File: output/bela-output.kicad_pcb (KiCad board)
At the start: 2 copper layers, 55 parts, among them P1 in_bela, P2 MTA-156-4, P3 out_mod, U1 TL074, U2 TL074, U3 TL072

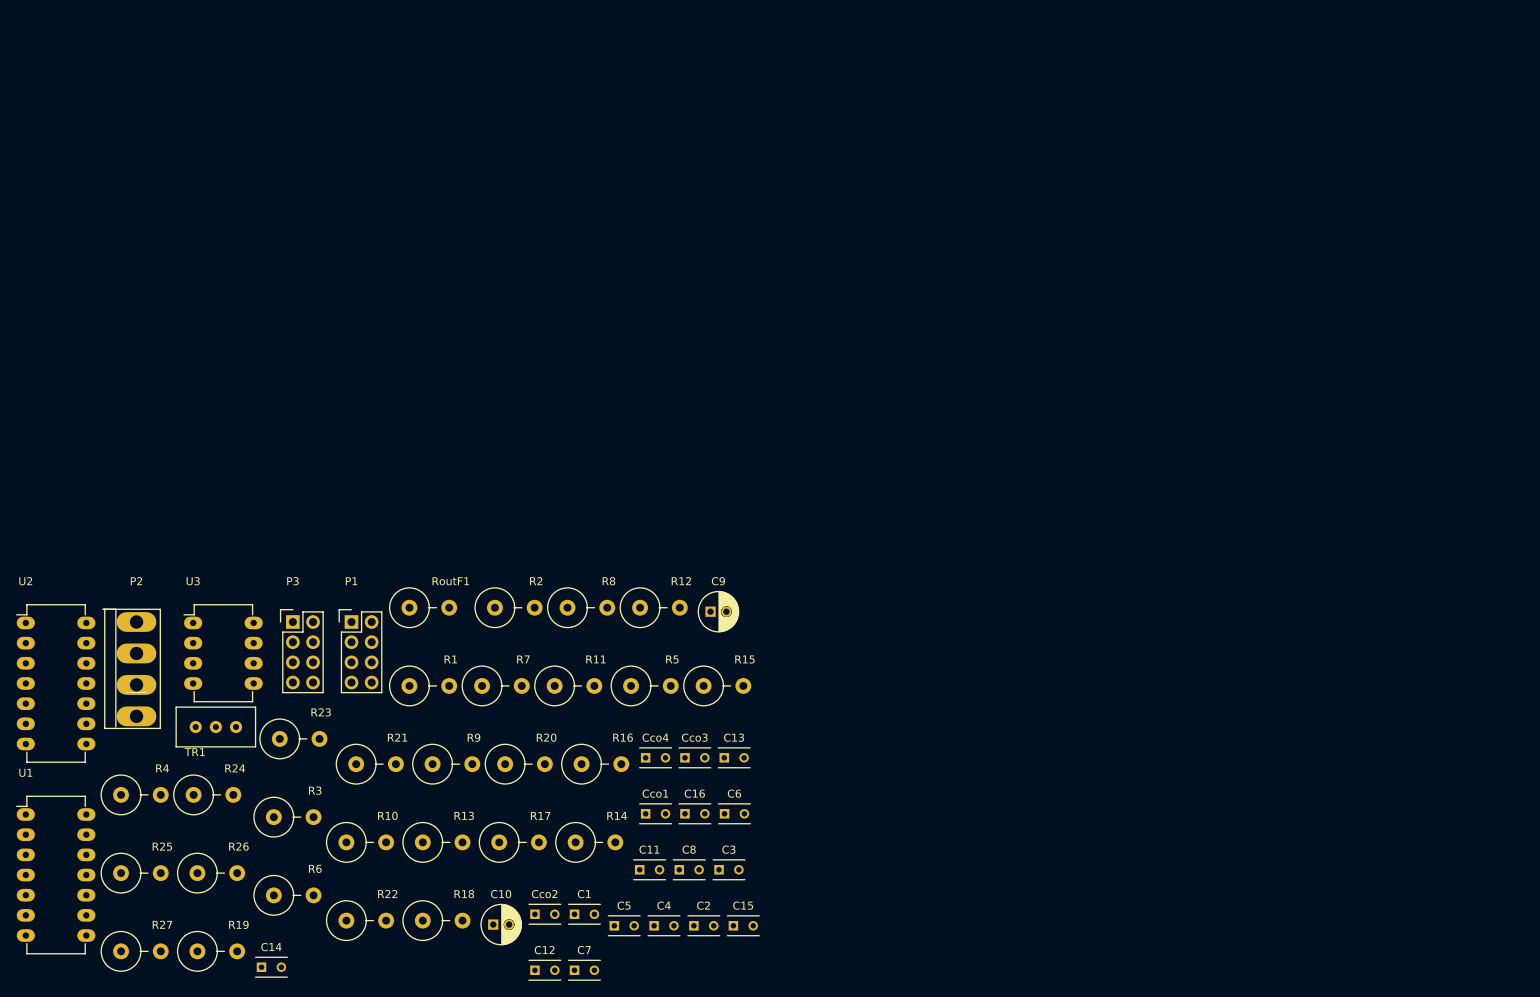
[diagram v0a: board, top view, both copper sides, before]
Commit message: mostly layed out, veridical resistors
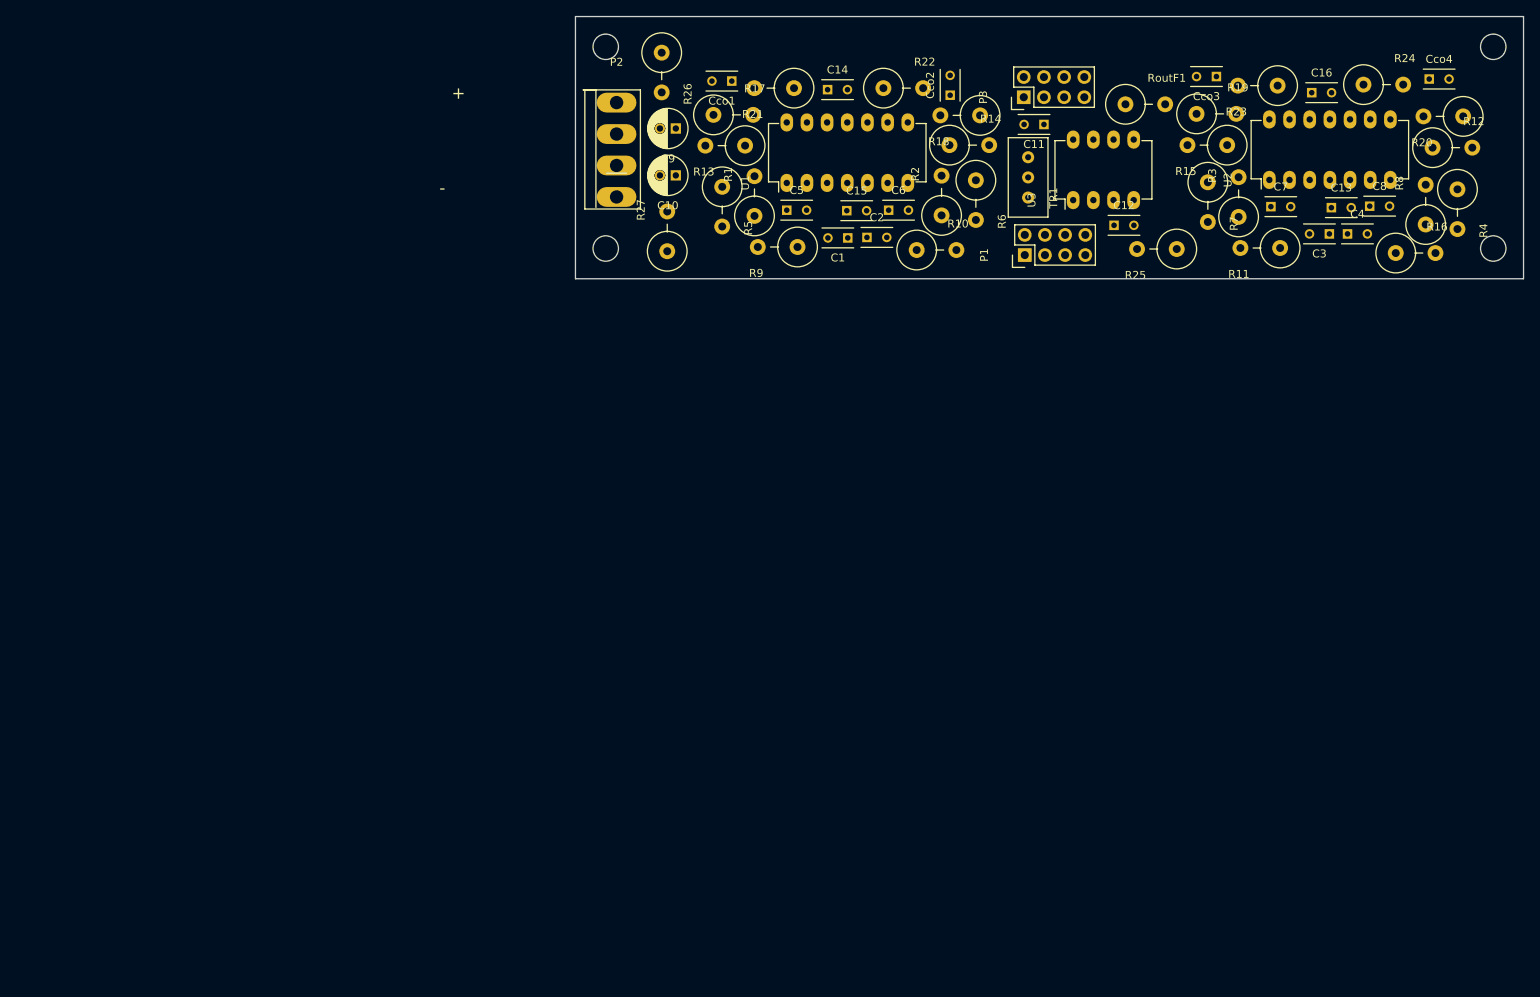
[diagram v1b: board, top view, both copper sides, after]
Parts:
- added REF1: MountingHole_3.2mm_M3, Mounting_Holes:MountingHole_3.2mm_M3, F.Cu at (105.4, 97.8)
- added REF2: MountingHole_3.2mm_M3, Mounting_Holes:MountingHole_3.2mm_M3, F.Cu at (105.4, 72.4)
- added REF3: MountingHole_3.2mm_M3, Mounting_Holes:MountingHole_3.2mm_M3, F.Cu at (217.2, 97.8)
- added REF4: MountingHole_3.2mm_M3, Mounting_Holes:MountingHole_3.2mm_M3, F.Cu at (217.2, 72.4)
- moved R4 181.5 mm to (212.7, 92.8), turned to 270 degrees
- moved R24 172.3 mm to (203.3, 77.2)
- moved U2 166.2 mm to (189.0, 89.2), turned to 90 degrees
- moved R19 164.2 mm to (182.3, 80.8)
- moved R25 150.1 mm to (174.8, 97.9), turned to 180 degrees
- moved R23 146.0 mm to (187.5, 77.3), turned to 180 degrees
- moved R3 142.3 mm to (185.1, 91.3), turned to 90 degrees
- moved R20 141.5 mm to (210.9, 81.2), turned to 180 degrees
- moved C14 131.5 mm to (133.3, 77.8)
- moved Cco4 130.5 mm to (209.1, 76.5)
- moved C7 130.1 mm to (189.2, 92.5)
- moved TR1 127.0 mm to (161.1, 88.8), turned to 90 degrees
- moved R22 124.7 mm to (142.9, 77.6)
- moved U1 124.5 mm to (128.2, 89.5), turned to 90 degrees
- moved C4 123.3 mm to (198.8, 95.9)
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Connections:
- R26 pad 1: Net-(P2-Pad1) -> VCC
- R26 pad 2: VCC -> Net-(P2-Pad1)
- U1 pad 10: Net-(C3-Pad2) -> Net-(R10-Pad1)
- U1 pad 12: Net-(C4-Pad2) -> Net-(R9-Pad1)
- U1 pad 13: Net-(C8-Pad1) -> Net-(R13-Pad2)
- U1 pad 14: Net-(C8-Pad1) -> Net-(Cco1-Pad2)
- U1 pad 8: Net-(C7-Pad1) -> Net-(Cco2-Pad2)
- U1 pad 9: Net-(C7-Pad1) -> Net-(R14-Pad2)
- U2 pad 1: Net-(Cco1-Pad2) -> Net-(C7-Pad1)
- U2 pad 10: Net-(R11-Pad1) -> Net-(R12-Pad1)
- U2 pad 12: Net-(R12-Pad1) -> Net-(R11-Pad1)
- U2 pad 13: Net-(R16-Pad2) -> Net-(R15-Pad2)
- U2 pad 14: Net-(Cco4-Pad2) -> Net-(Cco3-Pad2)
- U2 pad 2: Net-(R13-Pad2) -> Net-(C7-Pad1)
- U2 pad 3: Net-(R9-Pad1) -> Net-(C3-Pad2)
- U2 pad 5: Net-(R10-Pad1) -> Net-(C4-Pad2)
- U2 pad 6: Net-(R14-Pad2) -> Net-(C8-Pad1)
- U2 pad 7: Net-(Cco2-Pad2) -> Net-(C8-Pad1)
- U2 pad 8: Net-(Cco3-Pad2) -> Net-(Cco4-Pad2)
- U2 pad 9: Net-(R15-Pad2) -> Net-(R16-Pad2)
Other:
- board outline added: 119.4 x 33 mm
- board text added: "+"
- board text added: "-"
- board text added: "bela analog to mod"
- board text added: "http://x37v.info"
- board text added: "xnor 12/2016"

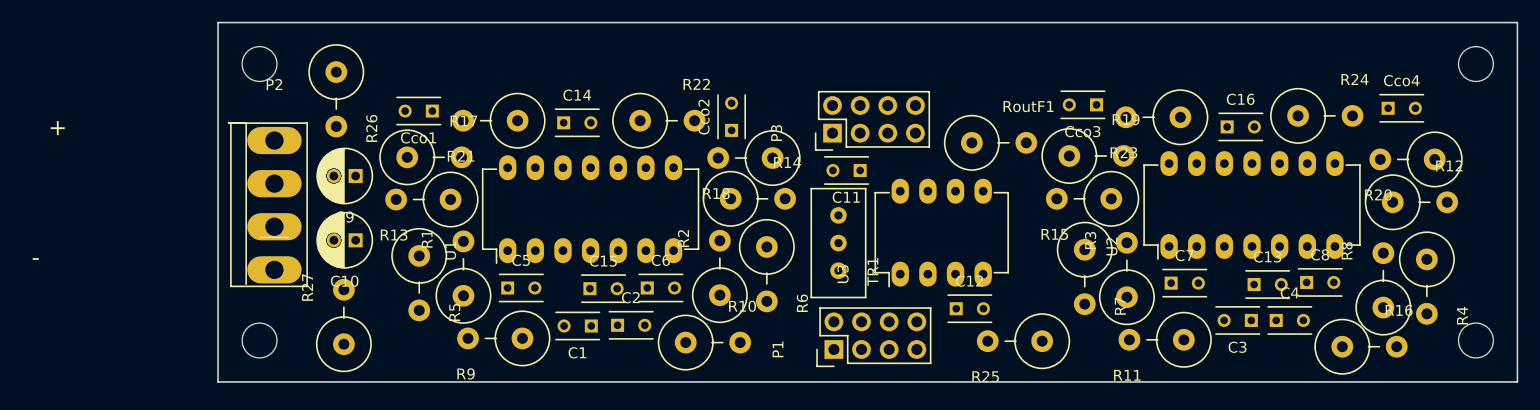
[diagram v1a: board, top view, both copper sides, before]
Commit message: flush resistor layout
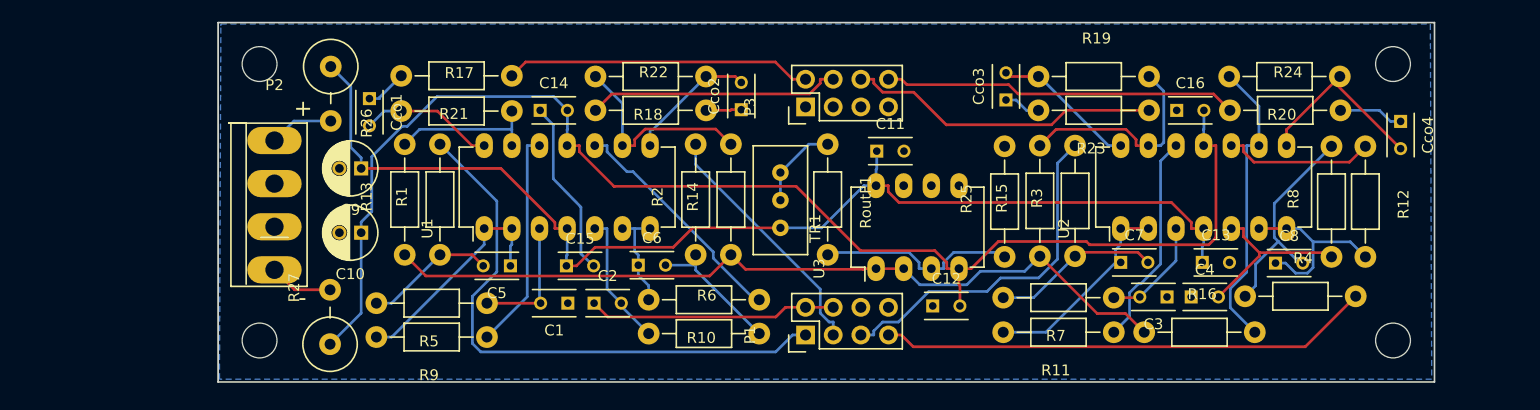
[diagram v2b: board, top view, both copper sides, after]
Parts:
- R1, R10, R11, R12, R13, R14, R15, R16, R17, R18, R19, R2, R20, R21, R22, R23, R24, R25, R3, R4, R5, R6, R7, R8, R9, RoutF1: footprint Resistors_ThroughHole:Resistor_Vertical_RM5mm -> Resistors_ThroughHole:Resistor_Horizontal_RM10mm
- moved R16 20.7 mm to (186.7, 97.0)
- moved R4 16.7 mm to (196.0, 93.7), turned to 0 degrees
- moved RoutF1 15.7 mm to (157.6, 79.8), turned to 270 degrees
- moved R6 12.2 mm to (141.2, 97.2), turned to 0 degrees
- moved R20 9.84 mm to (204.7, 73.5)
- moved R19 9.04 mm to (177.0, 73.5)
- moved R24 8.78 mm to (194.6, 76.6)
- moved Cco3 8.33 mm to (174.0, 75.7), turned to 90 degrees
- moved R18 8.32 mm to (146.4, 73.5)
- moved C4 8.10 mm to (191.0, 93.8)
- moved C3 8.04 mm to (188.8, 93.8)
- moved R25 7.81 mm to (173.9, 90.1), turned to 90 degrees
- moved REF3 7.62 mm to (209.6, 97.8)
- moved REF4 7.62 mm to (209.6, 72.4)
- moved R12 7.18 mm to (207.0, 79.9), turned to 270 degrees
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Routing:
- net VSS: track 0.00 -> 125.5 mm
- net VCC: track 0.00 -> 105.8 mm
- net outputoffset: track 0.00 -> 74.7 mm
- net bela_aout0: track 0.00 -> 53.0 mm
- net bela_aout3: track 0.00 -> 45.3 mm
- net GND: track 0.00 -> 39.2 mm
- net modular_aout3: track 0.00 -> 32.6 mm
- net bela_aout2: track 0.00 -> 32.3 mm
- net modular_aout2: track 0.00 -> 29.0 mm
- net modular_aout0: track 0.00 -> 28.2 mm
- net Net-(R16-Pad2): track 0.00 -> 27.3 mm
- net modular_aout1: track 0.00 -> 23.2 mm
- net bela_aout1: track 0.00 -> 23.0 mm
- net Net-(R10-Pad1): track 0.00 -> 21.6 mm
- net Net-(C5-Pad1): track 0.00 -> 20.9 mm
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- added copper zone on B.Cu, net GND
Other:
- board size 119.4 x 33 mm -> 111.8 x 33 mm

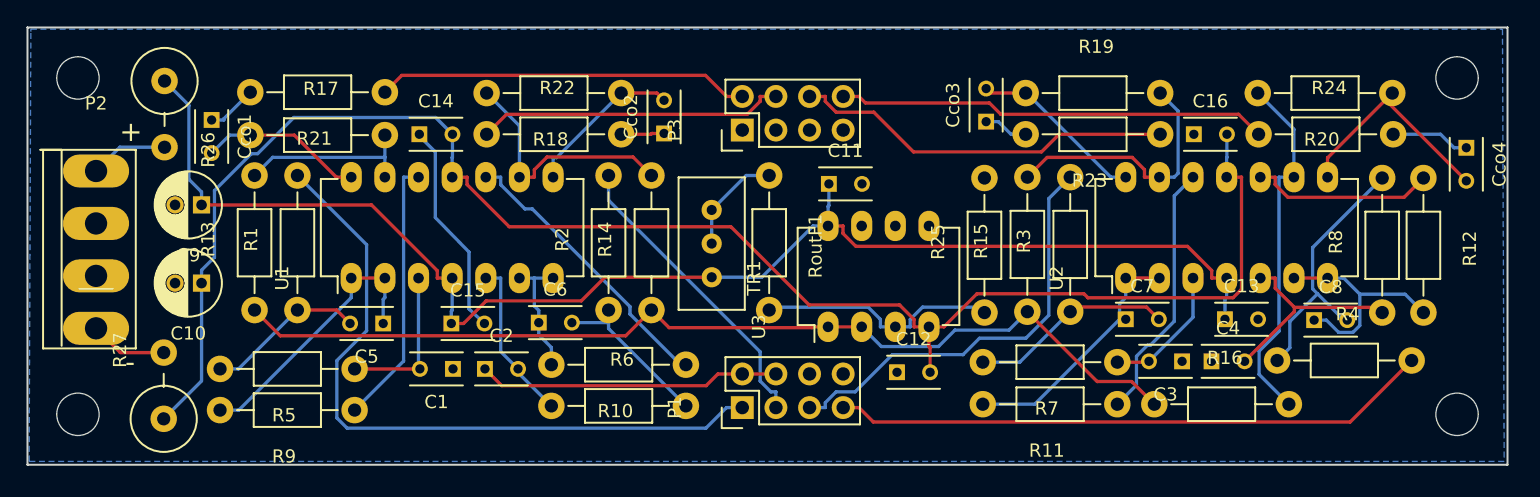
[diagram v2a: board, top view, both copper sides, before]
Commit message: added top filled gnd zone
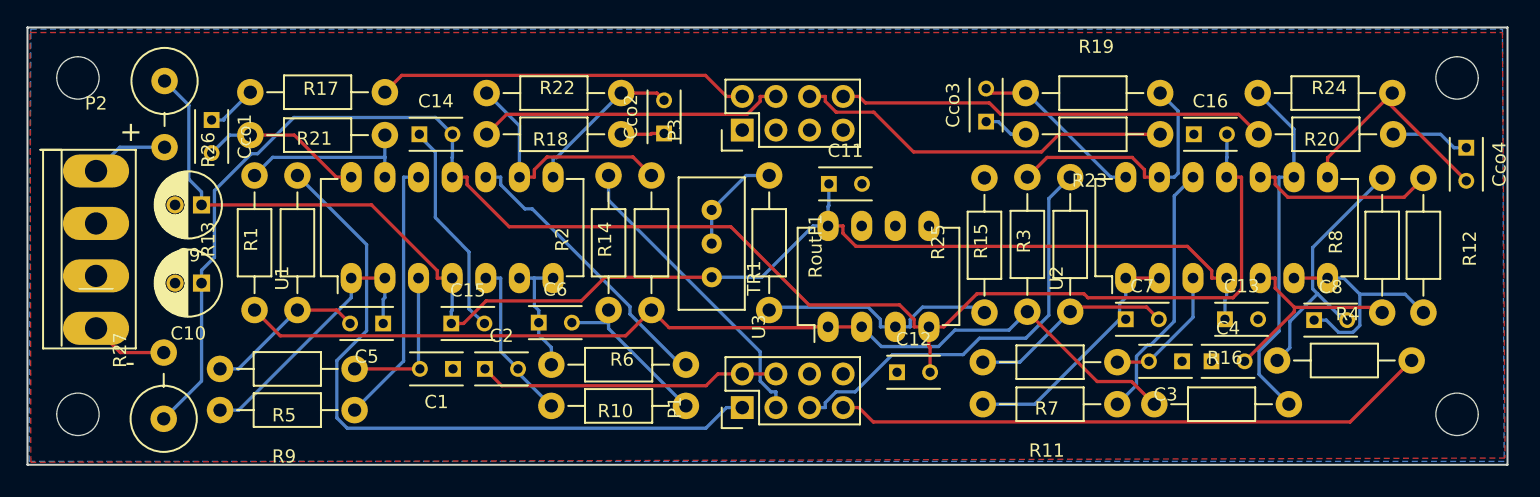
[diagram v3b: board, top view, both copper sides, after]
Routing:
- added copper zone on F.Cu, net GND
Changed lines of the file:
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@@
     (links 108)
     (no_connects 0)
-    (area 101.524999 68.504999 213.435001 101.675001)
+    (area 95.852857 67.215 219.107143 103.065)
     (thickness 1.6)
     (drawings 9)
@@
       )
     )
+  )
+  (zone (net 1) (net_name GND) (layer F.Cu) (hatch edge 0.508)
+    (connect_pads (clearance 0.508))
+    (min_thickness 0.254)
+    (fill yes (arc_segments 16) (thermal_gap 0.508) (thermal_bridge_width 0.508))
+    (polygon
+      (pts
+        (xy 101.854 68.961) (xy 212.979 68.961) (xy 213.1695 101.092) (xy 101.854 101.4095) (xy 101.7905 68.8975)
+      )
+    )

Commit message: moved text for output
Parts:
- C3, C4: value 220pF -> 220p
- C5, C6, C7, C8: value 440pF -> 440p
- moved R11 1.46 mm to (183.9, 98.5)
- moved R16 1.46 mm to (186.7, 98.5)
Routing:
- net bela_aout3: track 45.3 -> 48.4 mm
- net Net-(R11-Pad1): track 19.6 -> 20.8 mm
- net Net-(C7-Pad1): track 19.3 -> 20.3 mm
- net outputoffset: track 74.7 -> 75.3 mm
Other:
- board text added: "bela analog to modular"
- board text removed: "bela analog to mod"

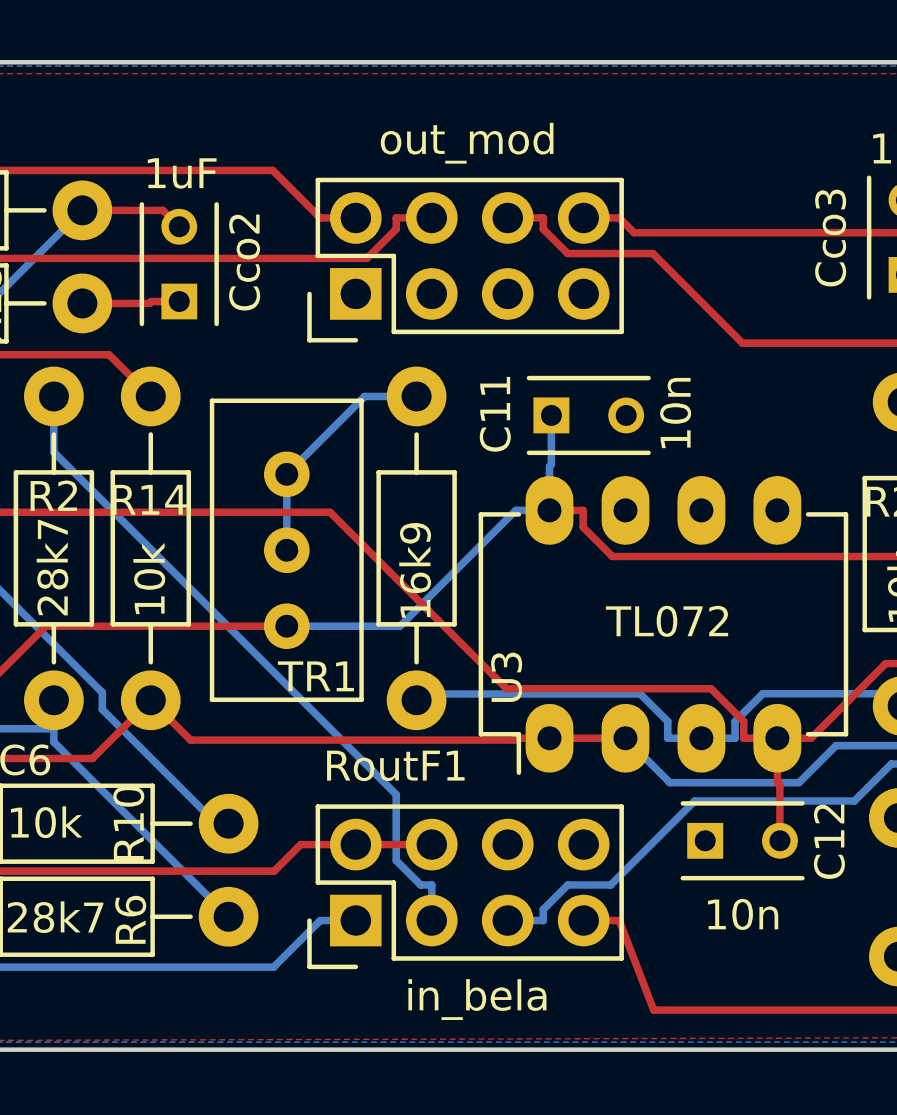
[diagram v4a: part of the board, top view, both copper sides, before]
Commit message: added gnd and 0 and 10k on trim
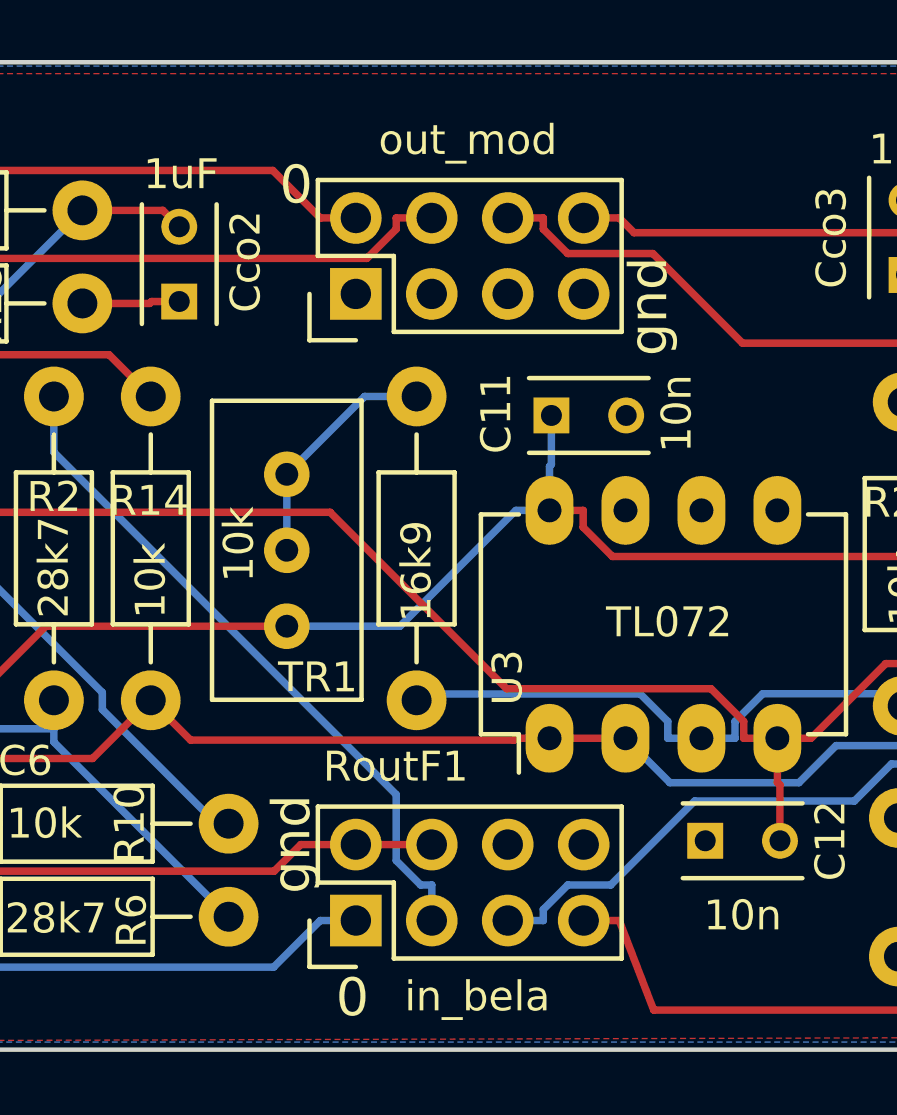
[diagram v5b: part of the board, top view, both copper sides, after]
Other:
- board text added: "0"
- board text added: "gnd"
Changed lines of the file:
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@@
     (area 95.852857 67.215 219.107143 103.065)
     (thickness 1.6)
-    (drawings 9)
+    (drawings 13)
     (tracks 319)
     (zones 0)
@@
   (page A4)
   (layers
-    (0 F.Cu signal)
-    (31 B.Cu signal)
+    (0 F.Cu signal hide)
+    (31 B.Cu signal hide)
     (32 B.Adhes user)
     (33 F.Adhes user)
@@
       (effects (font (size 1 1) (thickness 0.15)))
     )
-    (fp_text value 10k (at 0.2 -4.1 90) (layer F.SilkS) hide
+    (fp_text value 10k (at 0.2 -4.1 90) (layer F.SilkS)
       (effects (font (size 1 1) (thickness 0.15)))
     )
@@
       (net 29 "Net-(P2-Pad4)"))
   )
+  (gr_text gnd (at 165.3667 76.7461 90) (layer F.SilkS)
+    (effects (font (size 1.27 1.27) (thickness 0.254)))
+  )
+  (gr_text 0 (at 153.5811 72.6821) (layer F.SilkS)
+    (effects (font (size 1.27 1.27) (thickness 0.254)))
+  )
+  (gr_text 0 (at 155.4607 99.8601) (layer F.SilkS)
+    (effects (font (size 1.27 1.27) (thickness 0.254)))
+  )
+  (gr_text gnd (at 153.4287 94.7293 90) (layer F.SilkS)
+    (effects (font (size 1.27 1.27) (thickness 0.254)))
+  )
   (gr_text - (at 109.347 93.853) (layer F.SilkS)
